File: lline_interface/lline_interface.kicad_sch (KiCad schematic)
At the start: 7 parts, among them J1 Conn_02x05_Odd_Even, U1 LM393, U2 L7805

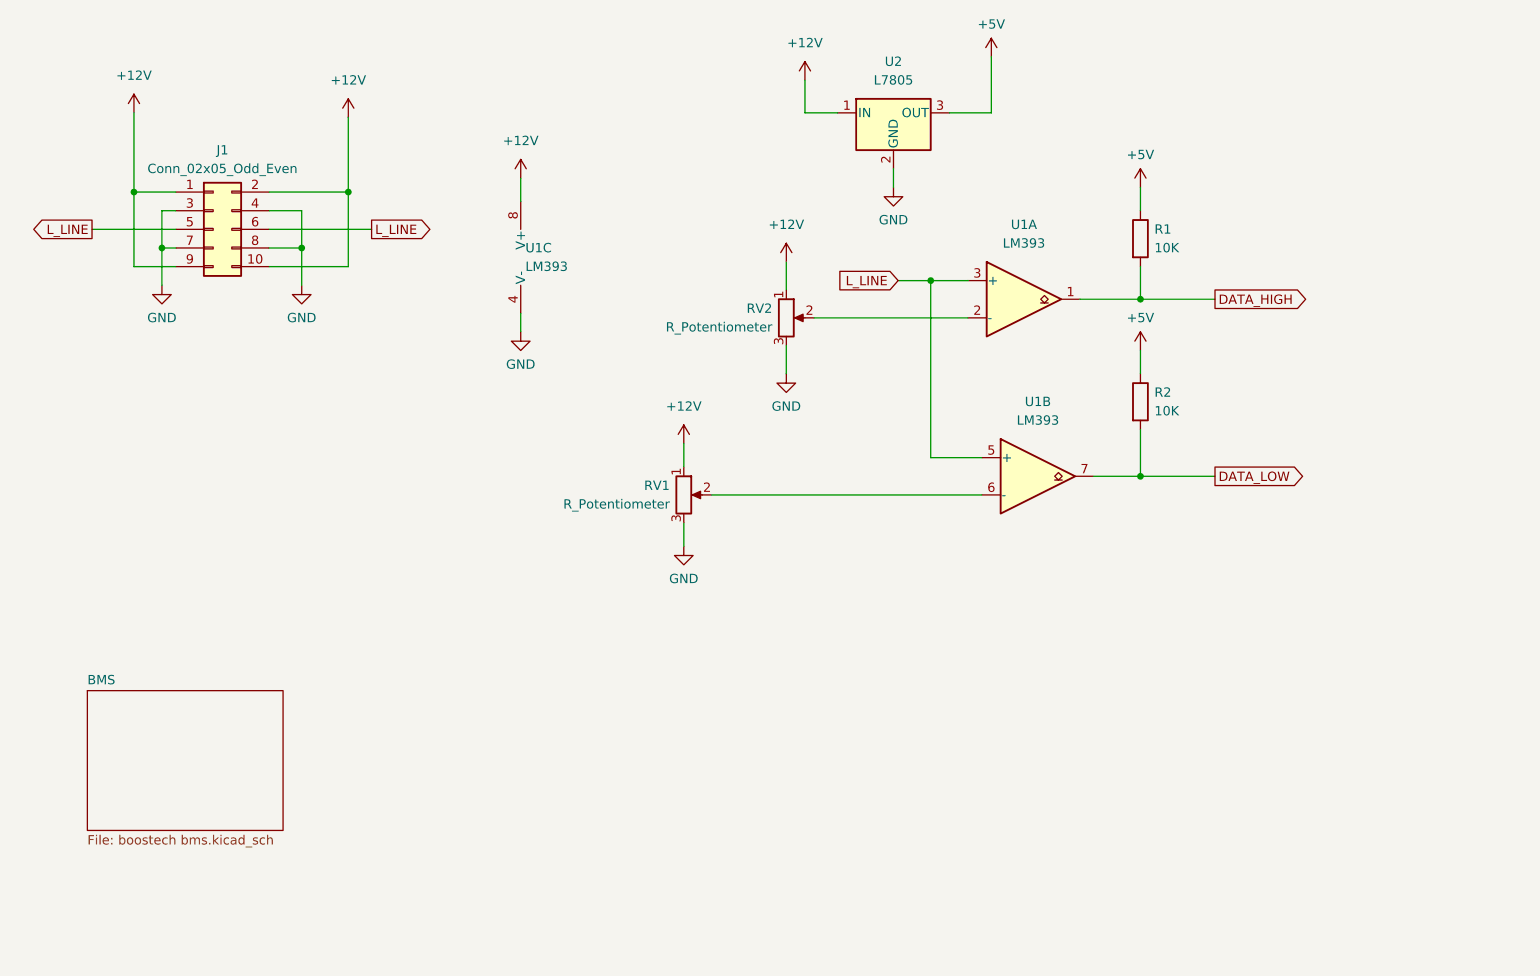
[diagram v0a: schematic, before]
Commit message: Start adding STM32 based master
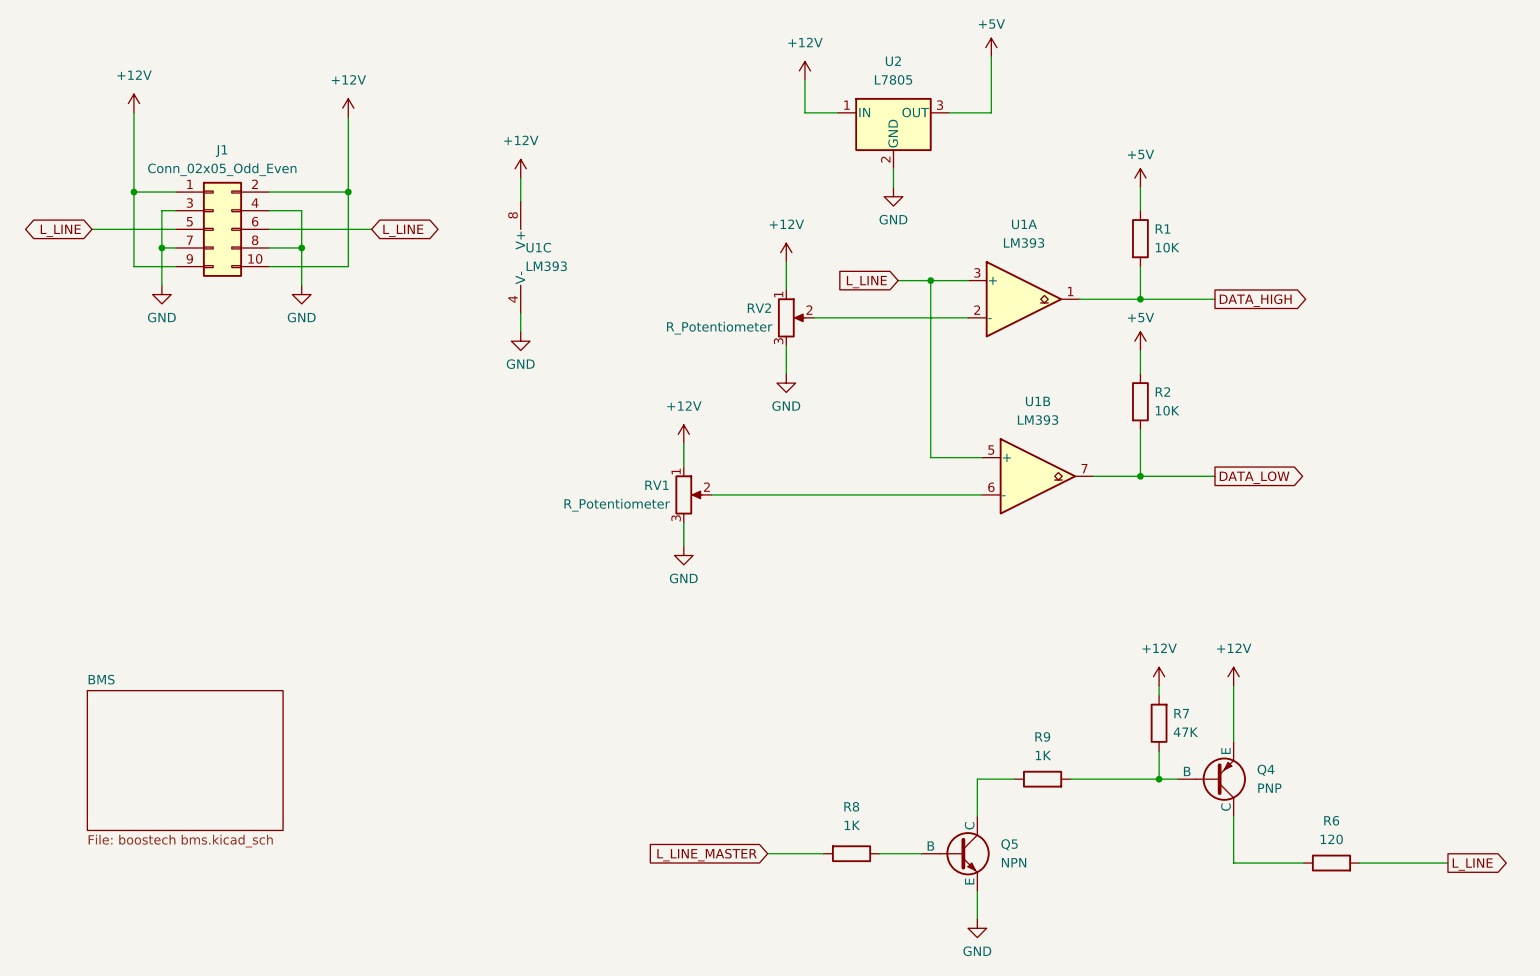
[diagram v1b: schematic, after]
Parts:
- added Q4: PNP, symbol Simulation_SPICE:PNP
- added Q5: NPN, symbol Simulation_SPICE:NPN
- added R6: 120, symbol Device:R
- added R7: 47K, symbol Device:R
- added R8, R9: 1K, symbol Device:R
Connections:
- net +12V: now also Q4.3 (E), R7.2
- net GND: now also Q5.3 (E)
- net L_LINE: now also R6.2
- new net: Q4.1 (C), R6.1
- new net: Q5.1 (C), R9.1
- new net: Q5.2 (B), R8.1
- new net: Q4.2 (B), R7.1, R9.2
- new net L_LINE_MASTER: R8.2
